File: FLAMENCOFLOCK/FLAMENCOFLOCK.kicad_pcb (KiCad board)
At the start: 2 copper layers, 31.8 x 31.8 mm, 6 parts, among them P2 ANTENNA, Q1 MOSFET_N

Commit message: finished FLAMENCOFLOCK
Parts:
- removed R1: DNP, GSG-0402
- removed R3, R4: 0, GSG-0402-SHORT-10MIL
- added J1: MINIDIN6, GSG-MD-6006, F.Cu at (95.0, 81.0)
- added J2: MINIDIN6, GSG-MD-6006, B.Cu at (95.0, 103.1)
- moved P2 48.5 mm to (106.9, 91.9), turned to 270 degrees
- moved R2 42.2 mm to (103.6, 94.4)
- moved Q1 38.7 mm to (104.5, 91.9)
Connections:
- Q1 pad S: /SOURCE -> GND
- R2 pad 2: /SOURCE -> GND
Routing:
- net /SHIELD: track 0.00 -> 47.8 mm
- net /GATE: track 0.00 -> 29.9 mm
- net N-000004: track 0.00 -> 15.7 mm
- net N-000001: track 0.00 -> 14.5 mm
- net N-000003: track 0.00 -> 9.50 mm
- net N-000002: track 0.00 -> 9.50 mm
- net GND: track 0.00 -> 4.96 mm
- net /DRAIN: track 0.00 -> 1.61 mm
- added copper zone on B.Cu, net GND
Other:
- net class Default: via_drill 0.635 -> 0.381
- rule via_min_drill: 0.508 -> 0.381

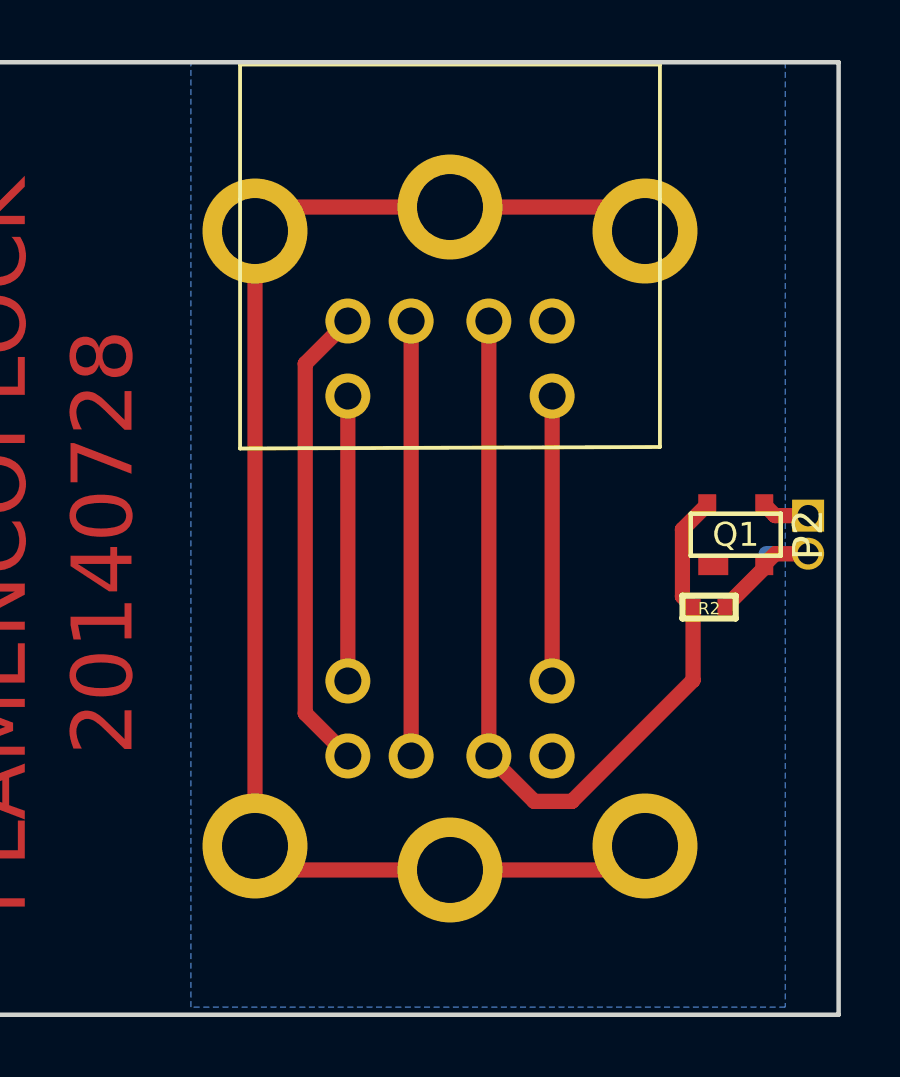
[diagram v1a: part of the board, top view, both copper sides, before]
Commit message: corrected PS/2 connector footprint (previous workaround was to mount on reverse side)
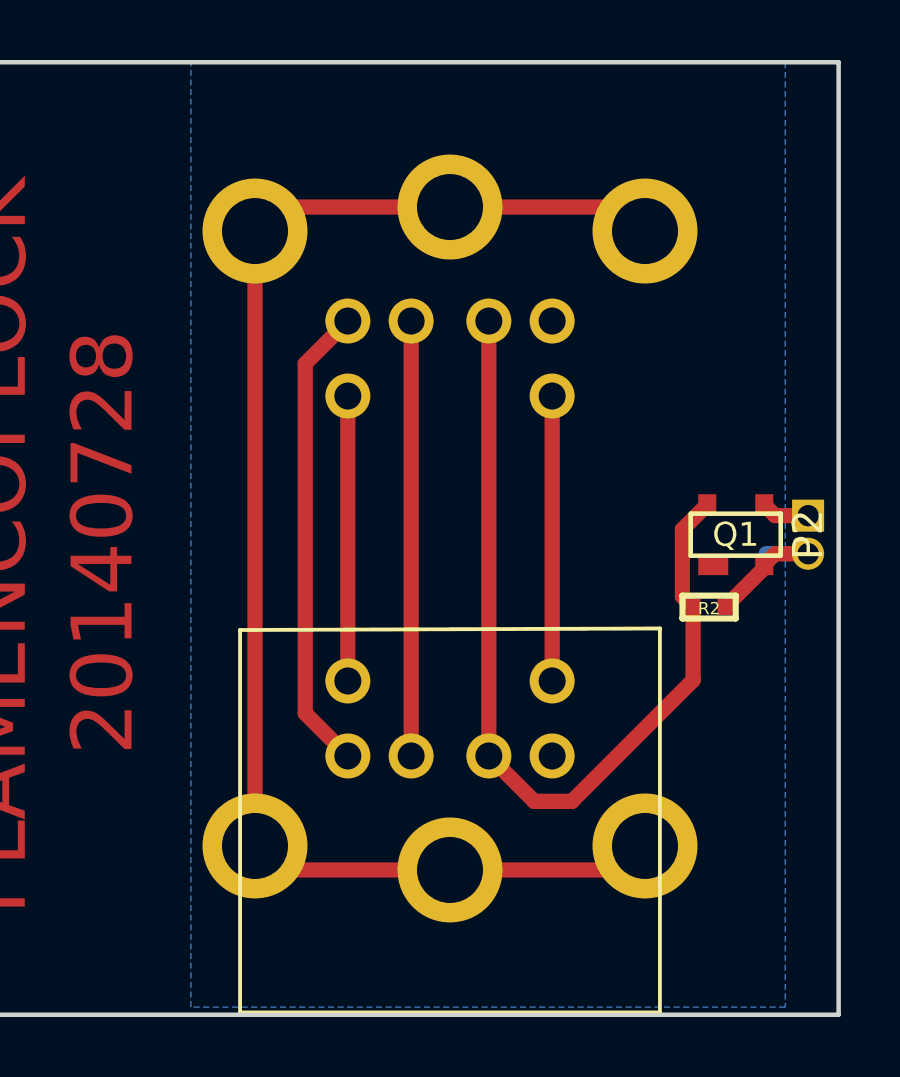
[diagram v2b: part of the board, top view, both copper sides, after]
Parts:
- J1: moved to B.Cu
- J2: moved to F.Cu
- turned J1 to 180 degrees
- turned J2 to 180 degrees
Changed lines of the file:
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@@
     (links 17)
     (no_connects 0)
-    (area 76.124999 76.124999 108.025001 108.025001)
+    (area 67.113453 75.958699 108.405555 108.191301)
     (thickness 1.6)
     (drawings 6)
@@
     (mod_text_size 1 1)
     (mod_text_width 0.15)
-    (pad_size 3.5 3.5)
-    (pad_drill 2.2)
+    (pad_size 1.5 1.5)
+    (pad_drill 0.9)
     (pad_to_mask_clearance 0.0762)
     (aux_axis_origin 0 0)
     (visible_elements FFFFFFBF)
     (pcbplotparams
-      (layerselection 284196865)
+      (layerselection 283672577)
       (usegerberextensions true)
       (excludeedgelayer true)
@@
     )
   )
+  (module GSG-MD-6006 (layer B.Cu)
+    (at 94.996 81.026 180)
+    (attr virtual)
+    (fp_text reference J1 (at 0 2.7 180) (layer B.SilkS)
+      (effects (font (size 0.8128 0.8128) (thickness 0.0889)) (justify mirror))
+    )
+    (fp_text value MINIDIN6 (at 0 4 180) (layer B.SilkS) hide
+      (effects (font (size 0.8128 0.8128) (thickness 0.0889)) (justify mirror))
+    )
+    (fp_line (start 6.9977 4.7498) (end -6.9977 4.7498) (layer B.SilkS) (width 0.127))
+    (fp_line (start -6.9977 4.7498) (end -6.9977 0.24892) (layer B.SilkS) (width 0.127))
+    (fp_line (start -6.9977 0.24892) (end -6.9977 -8.04926) (layer B.SilkS) (width 0.127))
+    (fp_line (start -6.9977 -8.04926) (end 6.9977 -7.99846) (layer B.SilkS) (width 0.127))
+    (fp_line (start 6.9977 -7.99846) (end 6.9977 -1.74752) (layer B.SilkS) (width 0.127))
+    (fp_line (start 6.9977 -1.74752) (end 6.9977 0.24892) (layer B.SilkS) (width 0.127))
+    (fp_line (start 6.9977 0.24892) (end 6.9977 4.7498) (layer B.SilkS) (width 0.127))
+    (pad 0 thru_hole circle (at 6.5 -0.8 180) (size 3.5 3.5) (drill 2.2)
+      (layers *.Cu *.Mask B.SilkS)
+      (net 3 /SHIELD)
+    )
+    (pad 0 thru_hole circle (at 0 0 180) (size 3.5 3.5) (drill 2.2)
+      (layers *.Cu *.Mask B.SilkS)
+      (net 3 /SHIELD)
+    )
+    (pad 0 thru_hole circle (at -6.5 -0.8 180) (size 3.5 3.5) (drill 2.2)
+      (layers *.Cu *.Mask B.SilkS)
+      (net 3 /SHIELD)
+    )
+    (pad 3 thru_hole circle (at -3.405 -3.8 180) (size 1.5 1.5) (drill 0.9)
+      (layers *.Cu *.Mask B.SilkS)
+      (net 4 GND)
+    )
+    (pad 6 thru_hole circle (at 3.405 -6.3 180) (size 1.5 1.5) (drill 0.9)
+      (layers *.Cu *.Mask B.SilkS)
+      (net 6 N-000002)
+    )
+    (pad 5 thru_hole circle (at -3.405 -6.3 180) (size 1.5 1.5) (drill 0.9)
+      (layers *.Cu *.Mask B.SilkS)
+      (net 7 N-000003)
+    )
+    (pad 2 thru_hole circle (at 1.295 -3.8 180) (size 1.5 1.5) (drill 0.9)
+      (layers *.Cu *.Mask B.SilkS)
+      (net 5 N-000001)
+    )
+    (pad 1 thru_hole circle (at -1.295 -3.8 180) (size 1.5 1.5) (drill 0.9)
+      (layers *.Cu *.Mask B.SilkS)
+      (net 2 /GATE)
+    )
+    (pad 4 thru_hole circle (at 3.405 -3.8 180) (size 1.5 1.5) (drill 0.9)
+      (layers *.Cu *.Mask B.SilkS)
+      (net 8 N-000004)
+    )
+  )
   (module GSG-MD-6006 (layer F.Cu)
-    (at 94.996 81.026)
+    (at 94.996 103.124 180)
     (attr virtual)
-    (fp_text reference J1 (at 0 -2.7) (layer B.SilkS)
+    (fp_text reference J2 (at 0 -2.7 180) (layer B.SilkS)
       (effects (font (size 0.8128 0.8128) (thickness 0.0889)))
     )
-    (fp_text value MINIDIN6 (at 0 -4) (layer B.SilkS) hide
+    (fp_text value MINIDIN6 (at 0 -4 180) (layer B.SilkS) hide
       (effects (font (size 0.8128 0.8128) (thickness 0.0889)))
     )
@@
     (fp_line (start 6.9977 1.74752) (end 6.9977 -0.24892) (layer F.SilkS) (width 0.127))
     (fp_line (start 6.9977 -0.24892) (end 6.9977 -4.7498) (layer F.SilkS) (width 0.127))
-    (pad 0 thru_hole circle (at 6.5 0.8) (size 3.5 3.5) (drill 2.2)
-      (layers *.Cu *.Mask F.SilkS)
-      (net 3 /SHIELD)
-    )
-    (pad 0 thru_hole circle (at 0 0) (size 3.5 3.5) (drill 2.2)
-      (layers *.Cu *.Mask F.SilkS)
-      (net 3 /SHIELD)
-    )
-    (pad 0 thru_hole circle (at -6.5 0.8) (size 3.5 3.5) (drill 2.2)
-      (layers *.Cu *.Mask F.SilkS)
-      (net 3 /SHIELD)
-    )
-    (pad 4 thru_hole circle (at -3.405 3.8) (size 1.5 1.5) (drill 0.9)
+    (pad 0 thru_hole circle (at 6.5 0.8 180) (size 3.5 3.5) (drill 2.2)
+      (layers *.Cu *.Mask F.SilkS)
+      (net 3 /SHIELD)
+    )
+    (pad 0 thru_hole circle (at 0 0 180) (size 3.5 3.5) (drill 2.2)
+      (layers *.Cu *.Mask F.SilkS)
+      (net 3 /SHIELD)
+    )
+    (pad 0 thru_hole circle (at -6.5 0.8 180) (size 3.5 3.5) (drill 2.2)
+      (layers *.Cu *.Mask F.SilkS)
+      (net 3 /SHIELD)
+    )
+    (pad 3 thru_hole circle (at -3.405 3.8 180) (size 1.5 1.5) (drill 0.9)
+      (layers *.Cu *.Mask F.SilkS)
+      (net 4 GND)
+    )
+    (pad 6 thru_hole circle (at 3.405 6.3 180) (size 1.5 1.5) (drill 0.9)
+      (layers *.Cu *.Mask F.SilkS)
+      (net 6 N-000002)
+    )
+    (pad 5 thru_hole circle (at -3.405 6.3 180) (size 1.5 1.5) (drill 0.9)
+      (layers *.Cu *.Mask F.SilkS)
+      (net 7 N-000003)
+    )
+    (pad 2 thru_hole circle (at 1.295 3.8 180) (size 1.5 1.5) (drill 0.9)
+      (layers *.Cu *.Mask F.SilkS)
+      (net 5 N-000001)
+    )
+    (pad 1 thru_hole circle (at -1.295 3.8 180) (size 1.5 1.5) (drill 0.9)
+      (layers *.Cu *.Mask F.SilkS)
+      (net 2 /GATE)
+    )
+    (pad 4 thru_hole circle (at 3.405 3.8 180) (size 1.5 1.5) (drill 0.9)
       (layers *.Cu *.Mask F.SilkS)
       (net 8 N-000004)
-    )
-    (pad 5 thru_hole circle (at 3.405 6.3) (size 1.5 1.5) (drill 0.9)
-      (layers *.Cu *.Mask F.SilkS)
-      (net 7 N-000003)
-    )
-    (pad 6 thru_hole circle (at -3.405 6.3) (size 1.5 1.5) (drill 0.9)
-      (layers *.Cu *.Mask F.SilkS)
-      (net 6 N-000002)
-    )
-    (pad 1 thru_hole circle (at 1.295 3.8) (size 1.5 1.5) (drill 0.9)
-      (layers *.Cu *.Mask F.SilkS)
-      (net 2 /GATE)
-    )
-    (pad 2 thru_hole circle (at -1.295 3.8) (size 1.5 1.5) (drill 0.9)
-      (layers *.Cu *.Mask F.SilkS)
-      (net 5 N-000001)
-    )
-    (pad 3 thru_hole circle (at 3.405 3.8) (size 1.5 1.5) (drill 0.9)
-      (layers *.Cu *.Mask F.SilkS)
-      (net 4 GND)
-    )
-  )
-  (module GSG-MD-6006 (layer B.Cu)
-    (at 94.996 103.124)
-    (attr virtual)
-    (fp_text reference J2 (at 0 2.7) (layer B.SilkS)
-      (effects (font (size 0.8128 0.8128) (thickness 0.0889)) (justify mirror))
-    )
-    (fp_text value MINIDIN6 (at 0 4) (layer B.SilkS) hide
-      (effects (font (size 0.8128 0.8128) (thickness 0.0889)) (justify mirror))
-    )
-    (fp_line (start 6.9977 4.7498) (end -6.9977 4.7498) (layer B.SilkS) (width 0.127))
-    (fp_line (start -6.9977 4.7498) (end -6.9977 0.24892) (layer B.SilkS) (width 0.127))
-    (fp_line (start -6.9977 0.24892) (end -6.9977 -8.04926) (layer B.SilkS) (width 0.127))
-    (fp_line (start -6.9977 -8.04926) (end 6.9977 -7.99846) (layer B.SilkS) (width 0.127))
-    (fp_line (start 6.9977 -7.99846) (end 6.9977 -1.74752) (layer B.SilkS) (width 0.127))
-    (fp_line (start 6.9977 -1.74752) (end 6.9977 0.24892) (layer B.SilkS) (width 0.127))
-    (fp_line (start 6.9977 0.24892) (end 6.9977 4.7498) (layer B.SilkS) (width 0.127))
-    (pad 0 thru_hole circle (at 6.5 -0.8) (size 3.5 3.5) (drill 2.2)
-      (layers *.Cu *.Mask B.SilkS)
-      (net 3 /SHIELD)
-    )
-    (pad 0 thru_hole circle (at 0 0) (size 3.5 3.5) (drill 2.2)
-      (layers *.Cu *.Mask B.SilkS)
-      (net 3 /SHIELD)
-    )
-    (pad 0 thru_hole circle (at -6.5 -0.8) (size 3.5 3.5) (drill 2.2)
-      (layers *.Cu *.Mask B.SilkS)
-      (net 3 /SHIELD)
-    )
-    (pad 4 thru_hole circle (at -3.405 -3.8) (size 1.5 1.5) (drill 0.9)
-      (layers *.Cu *.Mask B.SilkS)
-      (net 8 N-000004)
-    )
-    (pad 5 thru_hole circle (at 3.405 -6.3) (size 1.5 1.5) (drill 0.9)
-      (layers *.Cu *.Mask B.SilkS)
-      (net 7 N-000003)
-    )
-    (pad 6 thru_hole circle (at -3.405 -6.3) (size 1.5 1.5) (drill 0.9)
-      (layers *.Cu *.Mask B.SilkS)
-      (net 6 N-000002)
-    )
-    (pad 1 thru_hole circle (at 1.295 -3.8) (size 1.5 1.5) (drill 0.9)
-      (layers *.Cu *.Mask B.SilkS)
-      (net 2 /GATE)
-    )
-    (pad 2 thru_hole circle (at -1.295 -3.8) (size 1.5 1.5) (drill 0.9)
-      (layers *.Cu *.Mask B.SilkS)
-      (net 5 N-000001)
-    )
-    (pad 3 thru_hole circle (at 3.405 -3.8) (size 1.5 1.5) (drill 0.9)
-      (layers *.Cu *.Mask B.SilkS)
-      (net 4 GND)
     )
   )
@@
   (segment (start 106.934 91.313) (end 105.836 91.313) (width 0.508) (layer F.Cu) (net 1))
   (segment (start 105.836 91.313) (end 105.471 90.948) (width 0.508) (layer F.Cu) (net 1))
-  (segment (start 103.0986 94.361) (end 103.0986 96.7994) (width 0.508) (layer F.Cu) (net 2) (status 400000))
-  (segment (start 97.805 100.838) (end 96.291 99.324) (width 0.508) (layer F.Cu) (net 2) (status 800000))
+  (segment (start 103.0986 94.361) (end 103.0986 96.7994) (width 0.508) (layer F.Cu) (net 2))
+  (segment (start 97.805 100.838) (end 96.291 99.324) (width 0.508) (layer F.Cu) (net 2))
   (segment (start 99.06 100.838) (end 97.805 100.838) (width 0.508) (layer F.Cu) (net 2))
   (segment (start 103.0986 96.7994) (end 99.06 100.838) (width 0.508) (layer F.Cu) (net 2))

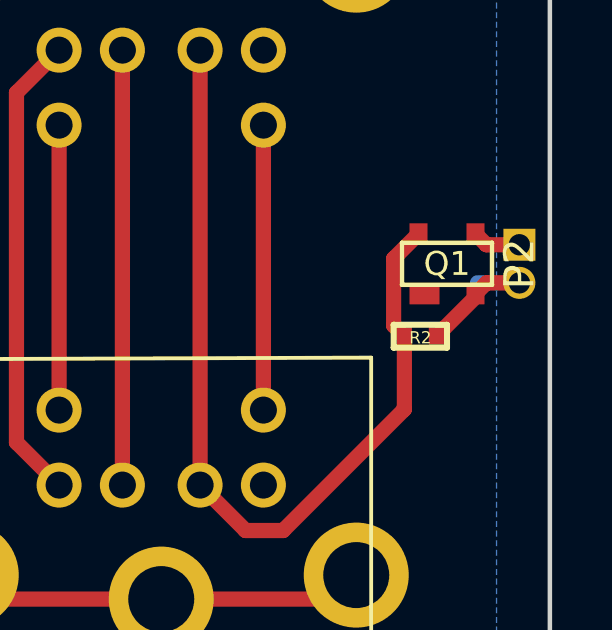
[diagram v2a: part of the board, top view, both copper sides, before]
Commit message: connected BSS83,215 substrate to source (previous workaround was solder blob)
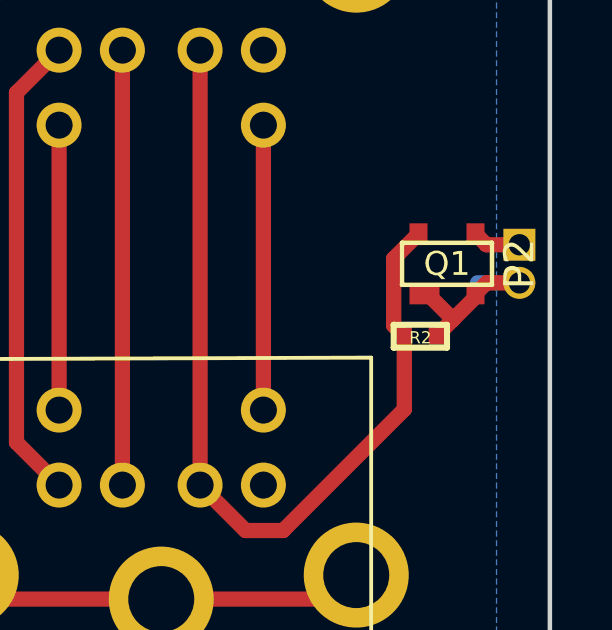
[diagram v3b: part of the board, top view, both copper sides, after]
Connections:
- Q1 pad B: (no net) -> GND
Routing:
- net GND: track 4.96 -> 6.27 mm
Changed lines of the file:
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@@
 (kicad_pcb (version 3) (host pcbnew "(2012-nov-02)-stable")
   (general
-    (links 17)
+    (links 18)
     (no_connects 0)
     (area 67.113453 75.958699 108.405555 108.191301)
     (thickness 1.6)
     (drawings 6)
-    (tracks 30)
+    (tracks 33)
     (zones 0)
     (modules 5)
@@
     (pad B smd rect (at -0.75 1) (size 1 0.7)
       (layers F.Cu F.Paste F.Mask)
+      (net 4 GND)
     )
     (pad S smd rect (at 0.95 1) (size 0.6 0.7)
@@
     (pad 6 thru_hole circle (at 3.405 -6.3 180) (size 1.5 1.5) (drill 0.9)
       (layers *.Cu *.Mask B.SilkS)
+      (net 8 N-000004)
+    )
+    (pad 5 thru_hole circle (at -3.405 -6.3 180) (size 1.5 1.5) (drill 0.9)
+      (layers *.Cu *.Mask B.SilkS)
       (net 6 N-000002)
     )
-    (pad 5 thru_hole circle (at -3.405 -6.3 180) (size 1.5 1.5) (drill 0.9)
+    (pad 2 thru_hole circle (at 1.295 -3.8 180) (size 1.5 1.5) (drill 0.9)
+      (layers *.Cu *.Mask B.SilkS)
+      (net 5 N-000001)
+    )
+    (pad 1 thru_hole circle (at -1.295 -3.8 180) (size 1.5 1.5) (drill 0.9)
+      (layers *.Cu *.Mask B.SilkS)
+      (net 2 /GATE)
+    )
+    (pad 4 thru_hole circle (at 3.405 -3.8 180) (size 1.5 1.5) (drill 0.9)
       (layers *.Cu *.Mask B.SilkS)
       (net 7 N-000003)
-    )
-    (pad 2 thru_hole circle (at 1.295 -3.8 180) (size 1.5 1.5) (drill 0.9)
-      (layers *.Cu *.Mask B.SilkS)
-      (net 5 N-000001)
-    )
-    (pad 1 thru_hole circle (at -1.295 -3.8 180) (size 1.5 1.5) (drill 0.9)
-      (layers *.Cu *.Mask B.SilkS)
-      (net 2 /GATE)
-    )
-    (pad 4 thru_hole circle (at 3.405 -3.8 180) (size 1.5 1.5) (drill 0.9)
-      (layers *.Cu *.Mask B.SilkS)
-      (net 8 N-000004)
     )
   )
@@
     (pad 6 thru_hole circle (at 3.405 6.3 180) (size 1.5 1.5) (drill 0.9)
       (layers *.Cu *.Mask F.SilkS)
+      (net 8 N-000004)
+    )
+    (pad 5 thru_hole circle (at -3.405 6.3 180) (size 1.5 1.5) (drill 0.9)
+      (layers *.Cu *.Mask F.SilkS)
       (net 6 N-000002)
     )
-    (pad 5 thru_hole circle (at -3.405 6.3 180) (size 1.5 1.5) (drill 0.9)
+    (pad 2 thru_hole circle (at 1.295 3.8 180) (size 1.5 1.5) (drill 0.9)
+      (layers *.Cu *.Mask F.SilkS)
+      (net 5 N-000001)
+    )
+    (pad 1 thru_hole circle (at -1.295 3.8 180) (size 1.5 1.5) (drill 0.9)
+      (layers *.Cu *.Mask F.SilkS)
+      (net 2 /GATE)
+    )
+    (pad 4 thru_hole circle (at 3.405 3.8 180) (size 1.5 1.5) (drill 0.9)
       (layers *.Cu *.Mask F.SilkS)
       (net 7 N-000003)
-    )
-    (pad 2 thru_hole circle (at 1.295 3.8 180) (size 1.5 1.5) (drill 0.9)
-      (layers *.Cu *.Mask F.SilkS)
-      (net 5 N-000001)
-    )
-    (pad 1 thru_hole circle (at -1.295 3.8 180) (size 1.5 1.5) (drill 0.9)
-      (layers *.Cu *.Mask F.SilkS)
-      (net 2 /GATE)
-    )
-    (pad 4 thru_hole circle (at 3.405 3.8 180) (size 1.5 1.5) (drill 0.9)
-      (layers *.Cu *.Mask F.SilkS)
-      (net 8 N-000004)
     )
   )
@@
   (segment (start 101.496 81.826) (end 100.696 81.026) (width 0.508) (layer F.Cu) (net 3))
   (segment (start 100.696 81.026) (end 94.996 81.026) (width 0.508) (layer F.Cu) (net 3))
-  (segment (start 104.1654 94.361) (end 105.471 93.0554) (width 0.508) (layer F.Cu) (net 4))
+  (segment (start 103.771 92.948) (end 103.87 92.948) (width 0.508) (layer F.Cu) (net 4))
+  (segment (start 103.87 92.948) (end 104.7242 93.8022) (width 0.508) (layer F.Cu) (net 4))
+  (segment (start 104.1654 94.361) (end 104.7242 93.8022) (width 0.508) (layer F.Cu) (net 4))
+  (segment (start 104.7242 93.8022) (end 105.471 93.0554) (width 0.508) (layer F.Cu) (net 4))
   (segment (start 105.471 93.0554) (end 105.471 92.948) (width 0.508) (layer F.Cu) (net 4))
   (segment (start 106.934 92.583) (end 105.836 92.583) (width 0.508) (layer F.Cu) (net 4))
@@
   (segment (start 106.934 92.583) (end 105.537 92.583) (width 0.508) (layer B.Cu) (net 4))
   (segment (start 93.701 84.826) (end 93.701 99.324) (width 0.508) (layer F.Cu) (net 5))
-  (segment (start 91.591 87.326) (end 91.591 96.824) (width 0.508) (layer F.Cu) (net 6))
-  (segment (start 98.401 87.326) (end 98.401 96.824) (width 0.508) (layer F.Cu) (net 7))
-  (segment (start 91.591 84.826) (end 90.17 86.247) (width 0.508) (layer F.Cu) (net 8))
-  (segment (start 90.17 97.903) (end 91.591 99.324) (width 0.508) (layer F.Cu) (net 8))
-  (segment (start 90.17 86.247) (end 90.17 97.903) (width 0.508) (layer F.Cu) (net 8))
+  (segment (start 98.401 87.326) (end 98.401 96.824) (width 0.508) (layer F.Cu) (net 6))
+  (segment (start 91.591 84.826) (end 90.17 86.247) (width 0.508) (layer F.Cu) (net 7))
+  (segment (start 90.17 97.903) (end 91.591 99.324) (width 0.508) (layer F.Cu) (net 7))
+  (segment (start 90.17 86.247) (end 90.17 97.903) (width 0.508) (layer F.Cu) (net 7))
+  (segment (start 91.591 87.326) (end 91.591 96.824) (width 0.508) (layer F.Cu) (net 8))
   (zone (net 4) (net_name GND) (layer B.Cu) (hatch edge 0.508)
     (connect_pads (clearance 0.254))
